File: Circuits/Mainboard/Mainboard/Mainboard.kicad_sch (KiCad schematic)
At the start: 71 parts, among them IC1 LM74500QDDFRQ1, IC2 LM74500QDDFRQ1, IC3 2536030320001, IC4 SX1280IMLTRT, IC5 SKY66122-11, IC6 TS2596CM533_RNG, IC7 TPS563300DRLR, J1 XT60PW-M, J10 B5P-VH_LF__SN_, J11 B6B-PH-K-S, J12 B5P-VH_LF__SN_, J13 B6B-PH-K-S, J14 B5P-VH_LF__SN_, J15 SMA-J-P-H-RA-TH1, J16 B5P-VH_LF__SN_, J2 XT60PW-M, J22 Conn_01x04_Pin, J23 Conn_01x04_Pin, J25 Conn_01x06_Pin, J26 Conn_01x04_Pin, J27 Conn_01x04_Pin, J3 Conn_01x06_Pin, J5 B6B-PH-K-S, J6 B5P-VH_LF__SN_, J7 B6B-PH-K-S, J8 Conn_01x06_Pin, J9 Conn_01x04_Pin, Q1 PSMN6R7-40MLDX, Q2 PSMN6R7-40MLDX, U1 NUCLEOH723ZG

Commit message: STP to pointer
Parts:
- removed C10: 10uF, 885012209073:CAPC3225X280N, symbol 885012209073:885012209073
- removed C13, C23, C7: 0.1uF, 885012007063:CAPC2012X90N, symbol 885012207098:885012207098
- removed C22: 470uF, Altium_WCAP-ASLL (rev24b):WCAP-ASLL_D16H17, symbol Altium_WCAP-ASLL (rev24b):865060663013
- removed D1: D_Schottky, symbol Device:D_Schottky
- removed IC6: TS2596CM533_RNG, TS2596CM533_RNG:TS2596CM550RNG, symbol TS2596CM533_RNG:TS2596CM533_RNG
- removed J17: ~, 61301021821:ESC_Adapter_socket, symbol 61301021821:6130XX21821_61301021821
- removed J22: Conn_01x04_Pin, Connector_PinHeader_2.54mm:PinHeader_1x04_P2.54mm_Vertical, symbol Connector:Conn_01x04_Pin
- removed L2: AMRM00101040470MA1, AMRM00101040470MA1:AMRM00101040470MA1, symbol AMRM00101040470MA1:AMRM00101040470MA1
- added C10, C22, C44: 0.1uF, Capacitor_SMD:C_0805_2012Metric_Pad1.18x1.45mm_HandSolder, symbol Device:C
- added C13, C7: 10uF, Capacitor_SMD:C_1210_3225Metric_Pad1.33x2.70mm_HandSolder, symbol Device:C
- added C23: 47uF, Capacitor_SMD:C_1210_3225Metric_Pad1.33x2.70mm_HandSolder, symbol Device:C
- added C29, C31, C33: 100nF, Capacitor_SMD:C_0805_2012Metric_Pad1.18x1.45mm_HandSolder, symbol Device:C
- added C30, C32, C34: 1nF, Capacitor_SMD:C_0805_2012Metric_Pad1.18x1.45mm_HandSolder, symbol Device:C
- added C35: 0p8, Capacitor_SMD:C_0805_2012Metric_Pad1.18x1.45mm_HandSolder, symbol Device:C
- added C36: 1p5, Capacitor_SMD:C_0805_2012Metric_Pad1.18x1.45mm_HandSolder, symbol Device:C
- added C37, C42: NA, Capacitor_SMD:C_0805_2012Metric_Pad1.18x1.45mm_HandSolder, symbol Device:C
- added C38: 0p5, Capacitor_SMD:C_0805_2012Metric_Pad1.18x1.45mm_HandSolder, symbol Device:C
- added C39: 100p, Capacitor_SMD:C_0805_2012Metric_Pad1.18x1.45mm_HandSolder, symbol Device:C
- added C40: 47p, Capacitor_SMD:C_0805_2012Metric_Pad1.18x1.45mm_HandSolder, symbol Device:C
- added C41: 0p6, Capacitor_SMD:C_0805_2012Metric_Pad1.18x1.45mm_HandSolder, symbol Device:C
- added C43: 4.7uF, Capacitor_SMD:C_0805_2012Metric_Pad1.18x1.45mm_HandSolder, symbol Device:C
- added FB1, FB2: 120R, symbol Device:FerriteBead_Small
- added IC6: TPS563300DRLR, TPS563300DRLR:TPS62932DRLR, symbol TPS563300DRLR:TPS563300DRLR
- added J17: Conn_01x04_Pin, Connector_PinHeader_2.54mm:PinHeader_1x04_P2.54mm_Vertical, symbol Connector:Conn_01x04_Pin
- added J22: ~, B-G431B-ESC1:ESC_Adapter_socket, symbol B-G431B-ESC1:B-G431B-ESC_Adapter_Pinout
- added L2: 5.6uH, Power Inductors - SMD WE-PD 5.6uH 6A:7447714220, symbol Device:L
- added P1: 66200621122, WR-MPC3 3.00 mm Male Header Dual Row Vertical:66200621122, symbol WR-MPC3 3.00 mm Male Header Dual Row Vertical:66200621122
- added R5: 3n, Resistor_SMD:R_0805_2012Metric, symbol Device:R
- added R6: 2n7, Resistor_SMD:R_0805_2012Metric, symbol Device:R
- added R7: 3n9, Resistor_SMD:R_0805_2012Metric, symbol Device:R
- added R8: 30.9kOhm, Resistor_SMD:R_0805_2012Metric_Pad1.20x1.40mm_HandSolder, symbol Device:R
- added R9: 10kOhm, Resistor_SMD:R_0805_2012Metric, symbol Altium_WRIS-RSKS (rev23a):560112120004
- added RN1: EXB-28V100JX, EXB28V510JX, symbol ESB-28V100:EXB-28V100JX
- added U2: ADP121-AUJZ28R7, ADP121-AUJZ28R7:UJ-5_ADI, symbol ADP121-AUJZ28R7:ADP121-AUJZ28R7
- added XTAL2: FW520WFMT1, CRYSTAL_FW520WFMT1_DIO, symbol FW520WFMT1:FW520WFMT1
- C1, C12, C14, C15, C17, C19, C2, C25, C26, C27, C3, C4, C6: footprint 885012007063:CAPC2012X90N -> Capacitor_SMD:C_0805_2012Metric_Pad1.18x1.45mm_HandSolder; symbol 885012207098:885012207098 -> Device:C
- C11, C24, C8, C9: footprint 885012209073:CAPC3225X280N -> Capacitor_SMD:C_1210_3225Metric_Pad1.33x2.70mm_HandSolder; symbol 885012209073:885012209073 -> Device:C
- C16, C18: footprint 885012007063:CAPC2012X90N -> Capacitor_SMD:C_0805_2012Metric_Pad1.18x1.45mm_HandSolder; symbol 885012007063:885012007063 -> Device:C
- C20, C21: footprint 885012007063:CAPC2012X90N -> Capacitor_SMD:C_0805_2012Metric_Pad1.18x1.45mm_HandSolder; symbol 885012207092:885012207092 -> Device:C
- C28: footprint Altium_WCAP-CSGP (rev24b):WCAP-CSGP_0805_L2W1.25H1.25 -> Capacitor_SMD:C_1210_3225Metric_Pad1.33x2.70mm_HandSolder; symbol Altium_WCAP-CSGP (rev24b):885012107006 -> Device:C
- C5: footprint 865080657018:CAPAE1030X1050N -> WCAP-ASLI Aluminum Electrolytic Capacitors:CAPAE1030X1050N; symbol 865080657018:865080657018 -> Device:C_Polarized
- J18, J19, J20, J21: footprint 61301021821:ESC_Adapter_socket -> B-G431B-ESC1:ESC_Adapter_socket; symbol 61301021821:6130XX21821_61301021821 -> B-G431B-ESC1:B-G431B-ESC_Adapter_Pinout; Category (none) -> Board-to-Board Connectors; ComponentLink1Description (none) -> Website Link; ComponentLink1URL (none) -> https://www.we-online.com/redexpert/article/61301021021?ad; ComponentLink2Description (none) -> Datasheet Link; ComponentLink2URL (none) -> https://www.we-online.com/redexpert/spec/61301021021?ad; Contact Resistance (none) -> 20mOhm; Gender (none) -> Pin Header; Manufacturer (none) -> Wurth Elektronik; Manufacturer Part Number (none) -> 61301021021; Match Code (none) -> WR-PHD; Mount (none) -> Through Hole; Number of Pins (none) -> 10; Number of Rows (none) -> 2; Operating Temperature Max (none) -> 105°C; Operating Temperature Min (none) -> -40°C; Orientation (none) -> Angled; Packaging (none) -> Bag; Pitch (none) -> 2.54mm; Rated Current (none) -> 3A; Withstanding Voltage (none) -> 500V; Working Voltage (none) -> 250V
- L1: footprint WE-HCC (rev24a):WE-HCC_1210 -> WE-HCC SMT High Current Cube Inductor:WE-HCC_1210; symbol WE-HCC (rev24a):7443330820 -> Device:L
- R3: footprint CRCW060352K3FKEA:RESC1608X50N -> Resistor_SMD:R_0805_2012Metric
- R4: footprint Altium_WRIS-RSKS (rev23a):WRIS-RSKS_0805_Wave -> Resistor_SMD:R_0805_2012Metric
- U1: symbol NUCLEO-H723ZG:NUCLEOH723ZG -> NUCLEOH723ZG:NUCLEOH723ZG
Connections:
- net 2.8V: now also C43.1, C44.1, U2.5 (VOUT)
- net 24V: now also J18.15, J18.16, J19.15, J19.16, J20.15, J20.16, J21.15, J21.16, C10.1, C7.1, IC6.3 (VIN), J22.13, J22.14, J22.15, J22.16
- net 3.3V: now also C12.1, U1.CN11_16 (3V3), C23.2, FB1.1, FB2.1, L2.2, R8.2; no longer C15.1, C16.1, C17.1, C18.1, IC4.15 (VBAT), U1.CN8_8 (D46/SDMMC_D3)
- net 5V: now also C28.1, J18.24, J18.27, J19.24, J19.27, J20.24, J20.27, J21.24, J21.27, C13.1, J17.1 (Pin_1), J22.24, J22.27, U2.1 (VIN), U2.3 (EN); no longer C28.2, J18.3 (L3), J18.4 (L4), J19.3 (L3), J19.4 (L4), J20.3 (L3), J20.4 (L4), J21.3 (L3), J21.4 (L4)
- net ADPS-9960_INT: now also U1.CN12_70 (PG6)
- net ADPS-9960_VL: now also U1.CN12_68 (PG5)
- net GND: now also C28.2, IC5.10 (GND_5), IC5.12 (GND_6), IC5.13 (GND_7), IC5.15 (GND_8), IC5.17 (GND_9), IC5.19 (GND_10), IC5.21 (GND_11), IC5.22 (GND_12), IC5.23 (GND_13), IC5.24 (GND_14), IC5.25 (GND_15), IC5.26 (GND_16), IC5.27 (GND_17), IC5.28 (GND_18), IC5.3 (GND_1), IC5.30 (GND_19), IC5.32 (GND_20), IC5.34 (GND_21), IC5.36 (GND_22), IC5.5 (GND_2), IC5.6 (GND_3), IC5.8 (GND_4), J15.2, J15.3, J15.4, J15.5, J18.17, J18.18, J18.19, J18.20, J18.26, J18.28, J19.17, J19.18, J19.19, J19.20, J19.26, J19.28, J20.17, J20.18, J20.19, J20.20, J20.26, J20.28, J21.17, J21.18, J21.19, J21.20, J21.26, J21.28, C10.2, C13.2, C23.1, C29.2, C30.2, C31.2, C32.2, C33.2, C34.2, C35.2, C36.2, C37.2, C41.1, C42.1, C43.2, C44.2, C7.2, IC6.4 (GND), J17.4 (Pin_4), J22.17, J22.18, J22.19, J22.20, J22.26, J22.28, R9.1, U2.2 (GND), XTAL2.2, XTAL2.4; no longer C28.1, J18.1 (L1), J18.11 (R1), J18.12 (R2), J18.2 (L2), J19.1 (L1), J19.11 (R1), J19.12 (R2), J19.2 (L2), J20.1 (L1), J20.11 (R1), J20.12 (R2), J20.2 (L2), J21.1 (L1), J21.11 (R1), J21.12 (R2), J21.2 (L2), U1.CN8_12 (D48/SDMMC_CMD), U1.CN8_14 (D49/IO)
- net M1_Encoder_A: now also J17.2 (Pin_2)
- net M1_Encoder_B: now also J17.3 (Pin_3)
- net M1_H1: now also J5.3, J22.23
- net M1_H2: now also J22.21
- net M1_H3: now also J22.22; no longer J5.3
- net M1_OUT1: now also J22.1, J22.2, J22.3, J22.4
- net M1_OUT2: now also J22.5, J22.6, J22.7, J22.8
- net M1_OUT3: now also J22.10, J22.11, J22.12, J22.9
- net M1_PWM: now also J22.30
- net M1_RX: now also J22.25
- net M1_TX: now also J22.29
- net M2_H1: now also J18.23; no longer J18.10 (L10)
- net M2_H2: now also J18.21; no longer J18.8 (L8)
- net M2_H3: now also J18.22; no longer J18.6 (L6)
- net M2_OUT1: now also J18.1, J18.2, J18.3, J18.4; no longer J18.19 (R9), J18.20 (R10)
- net M2_OUT2: now also J18.5, J18.6, J18.7, J18.8; no longer J18.17 (R7), J18.18 (R8)
- net M2_OUT3: now also J18.10, J18.11, J18.12, J18.9; no longer J18.15 (R5), J18.16 (R6)
- net M2_PWM: now also J18.30; no longer J18.9 (L9)
- net M2_RX: now also J18.25; no longer J18.7 (L7)
- net M2_TX: now also J18.29; no longer J18.5 (L5)
- net M3_H1: now also J19.23; no longer J19.10 (L10)
- net M3_H2: now also J19.21; no longer J19.8 (L8)
- net M3_H3: now also J19.22; no longer J19.6 (L6)
- net M3_OUT1: now also J19.1, J19.2, J19.3, J19.4; no longer J19.19 (R9), J19.20 (R10)
- net M3_OUT2: now also J19.5, J19.6, J19.7, J19.8; no longer J19.17 (R7), J19.18 (R8)
- net M3_OUT3: now also J19.10, J19.11, J19.12, J19.9; no longer J19.15 (R5), J19.16 (R6)
- net M3_PWM: now also J19.30; no longer J19.9 (L9)
- net M3_RX: now also J19.25; no longer J19.7 (L7)
- net M3_TX: now also J19.29; no longer J19.5 (L5)
- net M4_H1: now also J20.23; no longer J20.10 (L10)
- net M4_H2: now also J20.21; no longer J20.8 (L8)
- net M4_H3: now also J20.22; no longer J20.6 (L6)
- net M4_OUT1: now also J20.1, J20.2, J20.3, J20.4; no longer J20.19 (R9), J20.20 (R10)
- net M4_OUT2: now also J20.5, J20.6, J20.7, J20.8; no longer J20.17 (R7), J20.18 (R8)
- net M4_OUT3: now also J20.10, J20.11, J20.12, J20.9; no longer J20.15 (R5), J20.16 (R6)
- net M4_PWM: now also J20.30; no longer J20.9 (L9)
- net M4_RX: now also J20.25; no longer J20.7 (L7)
- net M4_TX: now also J20.29; no longer J20.5 (L5)
- net M5_OUT1: now also J21.1, J21.2, J21.3, J21.4; no longer J21.19 (R9), J21.20 (R10)
- net M5_OUT2: now also J21.5, J21.6, J21.7, J21.8; no longer J21.17 (R7), J21.18 (R8)
- net M5_OUT3: now also J21.10, J21.11, J21.12, J21.9; no longer J21.15 (R5), J21.16 (R6)
- net M5_PWM: now also J21.30; no longer J21.9 (L9)
- net M5_RX: now also J21.25; no longer J21.7 (L7)
- net M5_TX: now also J21.29; no longer J21.5 (L5)
- net SEN0374_BL-IND: now also U1.CN11_44 (PG3)
- net SEN0374_Boot: now also U1.CN12_46 (PD14)
- net SEN0374_INT: now also U1.CN12_41 (PD13)
- net SEN0374_PS1: now also U1.CN12_48 (PD15)
- net SEN0374_PS2: now also U1.CN11_42 (PG2)
- net SEN0374_RST: now also U1.CN12_69 (PG4)
- net VL53L4CD_INT: now also U1.CN12_58 (PF3)
- net VL53L4CD_SHUT: now also U1.CN11_52 (PF2)
- net VL6180_IO0: now also U1.CN12_2 (PC8)
- net VL6180_IO1: now also U1.CN12_66 (PG8)
- net RF_MISO: now reaches U1.CN11_35 (PC2)
- net RF_MISO: now also RN1.2
- net RF_MOSI: now reaches U1.CN11_37 (PC3)
- net RF_MOSI: now also RN1.1
- net at J15.1: now also C42.2, R7.2
- net at IC5.11 (CSD): now also IC5.29 (VCC2), IC5.31 (VCC0), IC5.33 (VCC1), C29.1, C30.1, C31.1, C32.1, C33.1, C34.1, FB2.2
- net at IC5.20 (ANT): now also C40.1
- net at IC5.4 (PA_IN): now also C39.2
- net at IC4.11 (VBAT_IO): now also C15.1, C16.1, C17.1, C18.1, IC4.15 (VBAT), IC4.3 (NRESET), FB1.2
- net at IC4.16 (MISO_TX): now also RN1.7
- net at IC4.17 (MOSI_RX): now also RN1.8
- net at IC4.18 (SCK_RTSN): now also RN1.6
- net at IC4.19 (NSS_CTS): now also RN1.5
- net at IC4.22 (RFIO): now also C35.1, R5.1
- net at IC4.4 (XTA): now also XTAL2.1
- net at IC4.6 (XTB): now also XTAL2.3
- net RF_SCK: now reaches U1.CN12_25 (PB10)
- net RF_SCK: now also RN1.3
- net RF_CS: now reaches U1.CN12_53 (PE15)
- net RF_CS: now also RN1.4
- new net: IC6.8 (FB), R8.1, R9.2
- new net: C40.2, C41.2, R7.1
- new net: C22.1, IC6.5 (SW), L2.1
- new net: C37.1, C38.2, C39.1, R6.2
- new net: C36.1, C38.1, R5.2, R6.1
- new net: C22.2, IC6.6 (BST)
- now unconnected: U1.CN11_10 (NC), U1.CN11_26 (NC), U1.CN11_67 (NC)
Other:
- note added: "Kicker board connector"
- note added: "boot"
- moved on the sheet: IC3, IC5, J10, J11, J12, J13, J14, J15, J16, J23, J25, J26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

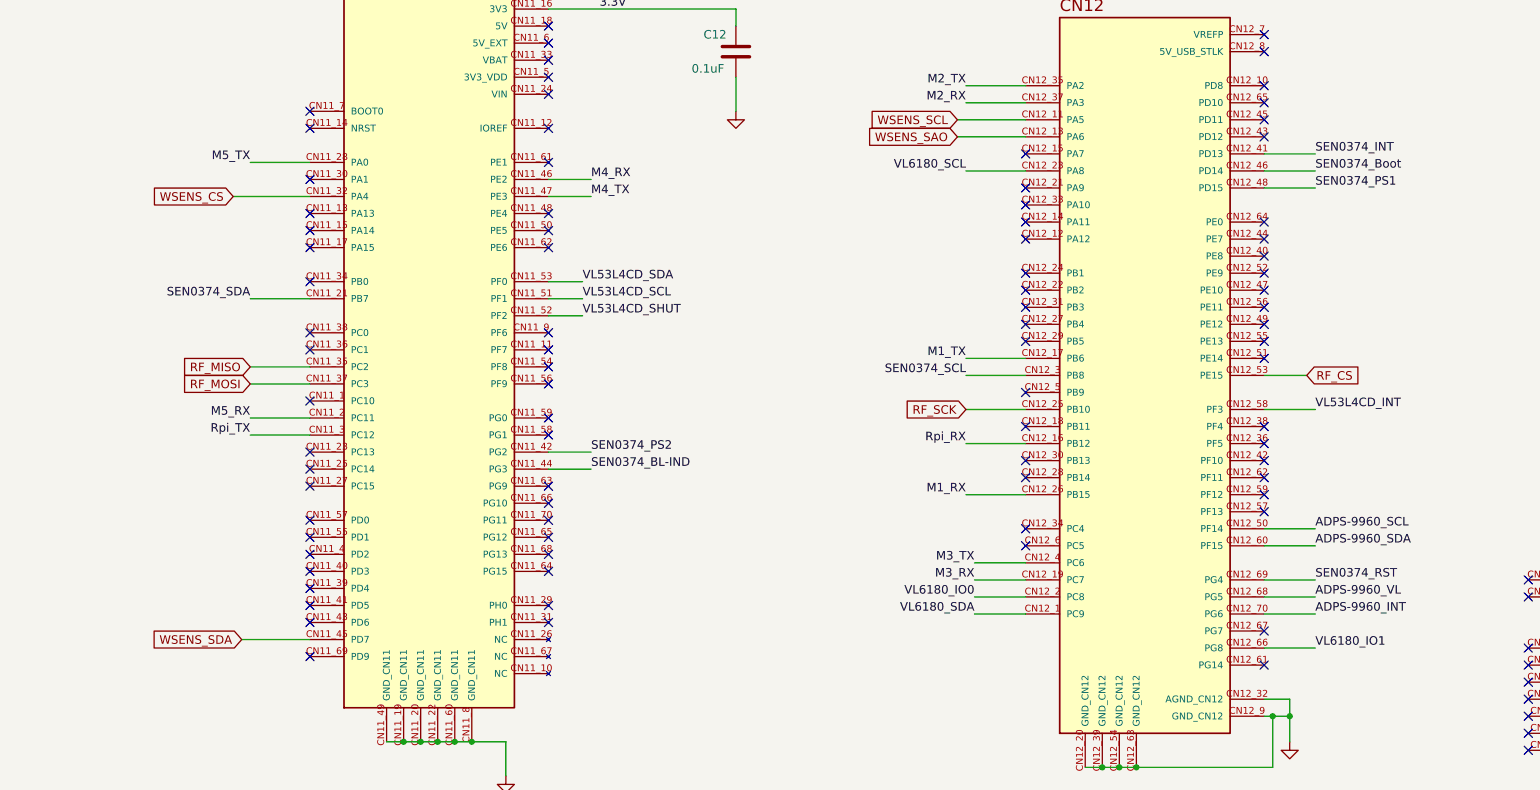
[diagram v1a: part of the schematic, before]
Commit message: Added updated pin configuration to stm32
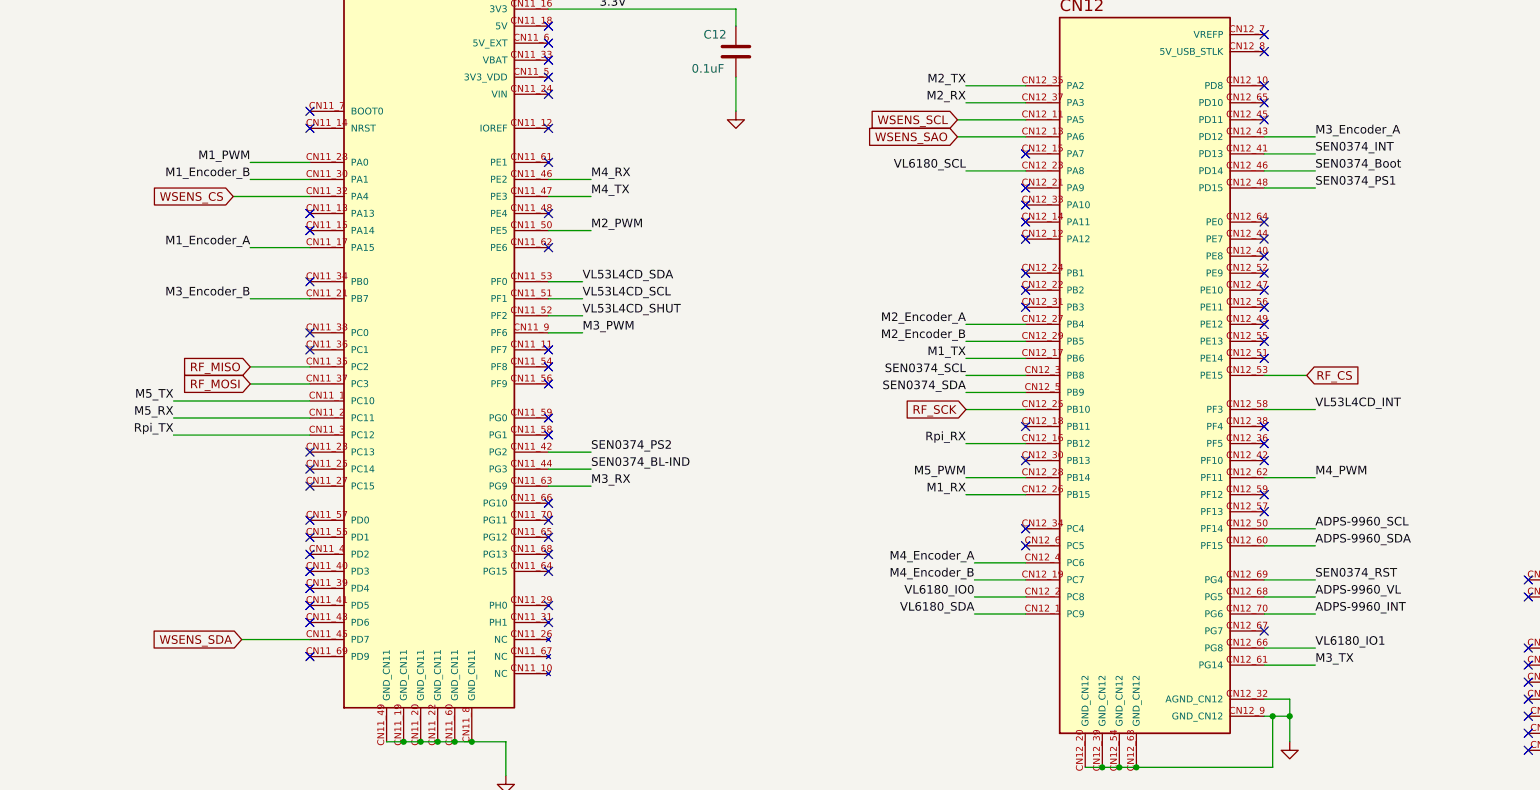
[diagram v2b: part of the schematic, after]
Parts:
- FB1, FB2: footprint (none) -> Resistor_SMD:R_0805_2012Metric_Pad1.20x1.40mm_HandSolder
- R1, R2, R3, R4, R5, R6, R7, R9: footprint Resistor_SMD:R_0805_2012Metric -> Resistor_SMD:R_0805_2012Metric_Pad1.20x1.40mm_HandSolder
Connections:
- net M1_Encoder_A: now also U1.CN11_17 (PA15)
- net M1_Encoder_B: now also U1.CN11_30 (PA1)
- net M1_PWM: now also U1.CN11_28 (PA0)
- net M2_Encoder_A: now also U1.CN12_27 (PB4)
- net M2_Encoder_B: now also U1.CN12_29 (PB5)
- net M2_PWM: now also U1.CN11_50 (PE5)
- net M3_Encoder_A: now also U1.CN12_43 (PD12)
- net M3_Encoder_B: now also U1.CN11_21 (PB7)
- net M3_PWM: now also U1.CN11_9 (PF6)
- net M3_RX: now also U1.CN11_63 (PG9); no longer U1.CN12_19 (PC7)
- net M3_TX: now also U1.CN12_61 (PG14); no longer U1.CN12_4 (PC6)
- net M4_Encoder_A: now also U1.CN12_4 (PC6)
- net M4_Encoder_B: now also U1.CN12_19 (PC7)
- net M4_PWM: now also U1.CN12_62 (PF11)
- net M5_PWM: now also U1.CN12_28 (PB14)
- net M5_TX: now also U1.CN11_1 (PC10); no longer U1.CN11_28 (PA0)
- net SEN0374_SDA: now also U1.CN12_5 (PB9); no longer U1.CN11_21 (PB7)
- no-connect marks 209 -> 196

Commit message: Added stm32cubemx project
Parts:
- added J24: Conn_01x06_Pin, Socket_header_6_pins_single_straight:61300611821, symbol Socket_header_6_pins_single_straight:61300611821
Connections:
- net 3.3V: now also J24.6
- net GND: now also J24.5
- net M3_OUT1: now also J12.2
- net M3_OUT3: no longer J12.2
- net RF_SCK: now also U1.CN11_40 (PD3); no longer U1.CN12_25 (PB10)
- net VL53L4CD_SCL: now also U1.CN12_25 (PB10); no longer U1.CN11_51 (PF1)
- net VL53L4CD_SDA: now also U1.CN12_18 (PB11); no longer U1.CN11_53 (PF0)
- net VL53L4CD2_SHUT: now reaches U1.CN12_36 (PF5)
- net VL53L4CD2_SHUT: now also J24.1
- net VL53L4CD2_INT: now reaches U1.CN12_38 (PF4)
- net VL53L4CD2_INT: now also J24.2
- new net VL53L4CD2_SCL: J24.3, U1.CN11_51 (PF1)
- new net VL53L4CD2_SDA: J24.4, U1.CN11_53 (PF0)
- no-connect marks 196 -> 192

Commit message: Routing tracks
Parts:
- removed C14: 0.1uF, Capacitor_SMD:C_0805_2012Metric_Pad1.18x1.45mm_HandSolder, symbol Device:C
- XTAL2: footprint CRYSTAL_FW520WFMT1_DIO -> FW520WFMT1:CRYSTAL_FW520WFMT1_DIO
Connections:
- net 3.3V: no longer U1.CN8_7 (3V3_CN8)
- net LT3751_GPIO_INPUT: now reaches P1.4
- net LT3751_GPIO_OUTPUT: now reaches P1.5
- no-connect marks 192 -> 194

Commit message: Mainborad routing
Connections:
- net GND: now also P1.1
- no-connect marks 194 -> 193
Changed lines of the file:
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@@
 	)
 	(no_connect
-		(at 537.21 54.61)
-	)
-	(no_connect
 		(at 638.81 313.69)
 	)
@@
 	(wire
 		(pts
+			(xy 524.51 55.88) (xy 524.51 54.61)
+		)
+		(stroke
+			(width 0)
+			(type default)
+		)
+	)
+	(wire
+		(pts
 			(xy 570.23 218.44) (xy 580.39 218.44)
 		)
@@
 	(wire
 		(pts
+			(xy 524.51 54.61) (xy 537.21 54.61)
+		)
+		(stroke
+			(width 0)
+			(type default)
+		)
+	)
+	(wire
+		(pts
 			(xy 276.86 146.05) (xy 284.48 146.05)
 		)
@@
 					(unit 1)
 				)
+			)
+		)
+	)
+	(symbol
+		(lib_id "power:GND")
+		(at 524.51 55.88 0)
+		(unit 1)
+		(exclude_from_sim no)
+		(in_bom yes)
+		(on_board yes)
+		(dnp no)
+		(fields_autoplaced yes)
+		(property "Reference" "#PWR023"
+			(at 524.51 62.23 0)
+			(effects
+				(font
+					(size 1.27 1.27)
+				)
+				(hide yes)
+			)
+		)
+		(property "Value" "GND"
+			(at 524.51 60.96 0)
+			(effects
+				(font
+					(size 1.27 1.27)
+				)
+				(hide yes)
+			)
+		)
+		(property "Footprint" ""
+			(at 524.51 55.88 0)
+			(effects
+				(font
+					(size 1.27 1.27)
+				)
+				(hide yes)
+			)
+		)
+		(property "Datasheet" ""
+			(at 524.51 55.88 0)
+			(effects
+				(font
+					(size 1.27 1.27)
+				)
+				(hide yes)
+			)
+		)
+		(property "Description" "Power symbol creates a global label with name \"GND\" , ground"
+			(at 524.51 55.88 0)
+			(effects
+				(font
+					(size 1.27 1.27)
+				)
+				(hide yes)
+			)
+		)
+		(pin "1"
+		)
+		(instances
+			(project "Mainboard"
+				(path "/778a7f39-1f28-457f-badd-61056e9c01e2"
+					(reference "#PWR023")
+					(unit 1)
+				)

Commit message: Exported mainboard, carrier board, and encoder to gerber
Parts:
- removed P1: 66200621122, WR-MPC3 3.00 mm Male Header Dual Row Vertical:66200621122, symbol WR-MPC3 3.00 mm Male Header Dual Row Vertical:66200621122
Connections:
- no-connect marks 193 -> 192
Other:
- note removed: "Kicker board connector"
- moved on the sheet: C12, J10, J11, J12, J13, J14, J16, J17, J18, J19, J20, J21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

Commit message: Exported gerber files
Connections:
- net 24V_1: now also J1.2; no longer J1.1
- net 24V_2: now also J2.2; no longer J2.1
- net GND: now also J1.1, J2.1; no longer J1.2, J2.2
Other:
- moved on the sheet: J1, J2

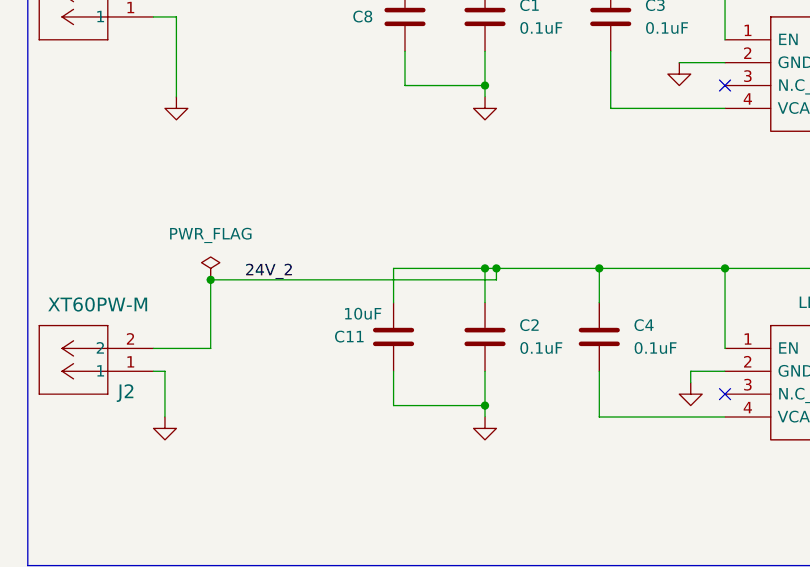
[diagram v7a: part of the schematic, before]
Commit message: Added 3 models to the pcbs
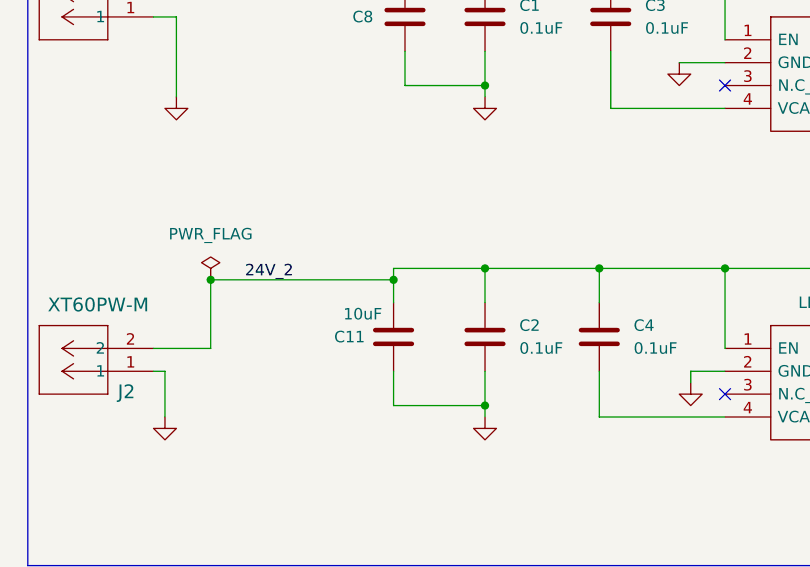
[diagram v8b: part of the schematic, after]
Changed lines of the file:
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@@
 	)
 	(junction
+		(at 59.69 133.35)
+		(diameter 0)
+		(color 0 0 0 0)
+	)
+	(junction
 		(at 129.54 135.89)
 		(diameter 0)
@@
 	)
 	(junction
-		(at 71.12 132.08)
-		(diameter 0)
-		(color 0 0 0 0)
-	)
-	(junction
 		(at 196.85 196.85)
 		(diameter 0)
@@
 	(wire
 		(pts
-			(xy 59.69 132.08) (xy 59.69 135.89)
-		)
-		(stroke
-			(width 0)
-			(type default)
-		)
-	)
-	(wire
-		(pts
 			(xy 82.55 243.84) (xy 151.13 243.84)
 		)
@@
 	(wire
 		(pts
-			(xy 71.12 133.35) (xy 71.12 132.08)
-		)
-		(stroke
-			(width 0)
-			(type default)
-		)
-	)
-	(wire
-		(pts
 			(xy 613.41 106.68) (xy 622.3 106.68)
 		)
@@
 	(wire
 		(pts
+			(xy 69.85 132.08) (xy 82.55 132.08)
+		)
+		(stroke
+			(width 0)
+			(type default)
+		)
+	)
+	(wire
+		(pts
 			(xy 177.8 229.87) (xy 190.5 229.87)
 		)
@@
 	(wire
 		(pts
-			(xy 39.37 133.35) (xy 71.12 133.35)
+			(xy 39.37 133.35) (xy 59.69 133.35)
 		)
 		(stroke
@@
 	(wire
 		(pts
-			(xy 69.85 132.08) (xy 59.69 132.08)
-		)
-		(stroke
-			(width 0)
-			(type default)
-		)
-	)
-	(wire
-		(pts
 			(xy 226.06 194.31) (xy 226.06 196.85)
 		)
@@
 	(wire
 		(pts
+			(xy 59.69 133.35) (xy 59.69 135.89)
+		)
+		(stroke
+			(width 0)
+			(type default)
+		)
+	)
+	(wire
+		(pts
 			(xy 77.47 176.53) (xy 77.47 186.69)
 		)
@@
 	(wire
 		(pts
+			(xy 59.69 132.08) (xy 59.69 133.35)
+		)
+		(stroke
+			(width 0)
+			(type default)
+		)
+	)
+	(wire
+		(pts
 			(xy 110.49 209.55) (xy 110.49 217.17)
 		)
@@
 	(wire
 		(pts
+			(xy 59.69 132.08) (xy 69.85 132.08)
+		)
+		(stroke
+			(width 0)
+			(type default)
+		)
+	)
+	(wire
+		(pts
 			(xy 302.26 96.52) (xy 281.94 96.52)
 		)
@@
 	(wire
 		(pts
-			(xy 71.12 132.08) (xy 82.55 132.08)
-		)
-		(stroke
-			(width 0)
-			(type default)
-		)
-	)
-	(wire
-		(pts
 			(xy 82.55 143.51) (xy 82.55 148.59)
 		)
@@
 		)
 		(stroke
-			(width 0)
-			(type default)
-		)
-	)
-	(wire
-		(pts
-			(xy 69.85 132.08) (xy 71.12 132.08)
-		)
-		(stroke
